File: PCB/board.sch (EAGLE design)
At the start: 43 parts, among them J1 USB-A_PTH_MALE, U1 CH340E, U2 NRF52832, Y1 32MHz_2016, Y2 32.768kHz

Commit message: output files, dir cleanup
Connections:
- net UART_RX: now also U1.RX; no longer U1.TX
- net UART_TX: now also U1.TX; no longer U1.RX
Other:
- moved on the sheet: D1
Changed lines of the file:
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@@
 </classes>
 <parts>
-<part name="SUPPLY2" library="angrypig7-Symbols" deviceset="3V3" device=""/>
-<part name="GND1" library="angrypig7-Symbols" deviceset="GND" device=""/>
-<part name="SUPPLY3" library="angrypig7-Symbols" deviceset="5V" device=""/>
-<part name="SUPPLY4" library="angrypig7-Symbols" deviceset="VIN" device=""/>
-<part name="GND2" library="angrypig7-Symbols" deviceset="GND" device=""/>
-<part name="GND3" library="angrypig7-Symbols" deviceset="GND" device=""/>
 <part name="U2" library="angrypig7-IC-MCU" deviceset="NRF52832" device="" package3d_urn="urn:adsk.eagle:package:25776865/5">
 <attribute name="JLC_ROTATION" value="270"/>
@@
 </plain>
 <instances>
-<instance part="SUPPLY2" gate="G$1" x="27.94" y="21.59" smashed="yes">
-<attribute name="VALUE" x="27.94" y="24.384" size="1.778" layer="96" align="bottom-center"/>
-</instance>
-<instance part="GND1" gate="1" x="27.94" y="15.24" smashed="yes">
-<attribute name="VALUE" x="27.94" y="12.446" size="1.778" layer="96" align="top-center"/>
-</instance>
-<instance part="SUPPLY3" gate="G$1" x="21.59" y="21.59" smashed="yes">
-<attribute name="VALUE" x="21.59" y="24.384" size="1.778" layer="96" align="bottom-center"/>
-</instance>
-<instance part="SUPPLY4" gate="G$1" x="15.24" y="21.59" smashed="yes">
-<attribute name="VALUE" x="15.24" y="24.384" size="1.778" layer="96" align="bottom-center"/>
-</instance>
-<instance part="GND2" gate="1" x="21.59" y="15.24" smashed="yes">
-<attribute name="VALUE" x="21.59" y="12.446" size="1.778" layer="96" align="top-center"/>
-</instance>
-<instance part="GND3" gate="1" x="15.24" y="15.24" smashed="yes">
-<attribute name="VALUE" x="15.24" y="12.446" size="1.778" layer="96" align="top-center"/>
-</instance>
 <instance part="J1" gate="G$1" x="102.87" y="199.39" smashed="yes">
 <attribute name="NAME" x="97.79" y="209.804" size="1.778" layer="95" font="vector"/>
@@
 <attribute name="LCSC" x="102.87" y="199.39" size="1.778" layer="96" display="off"/>
 </instance>
-<instance part="SUPPLY1" gate="G$1" x="157.48" y="212.09" smashed="yes">
-<attribute name="VALUE" x="157.48" y="214.884" size="1.778" layer="96" align="bottom-center"/>
+<instance part="SUPPLY1" gate="G$1" x="157.48" y="214.63" smashed="yes">
+<attribute name="VALUE" x="157.48" y="217.424" size="1.778" layer="96" align="bottom-center"/>
 </instance>
 <instance part="GND4" gate="1" x="120.65" y="190.5" smashed="yes">
@@
 <attribute name="VALUE" x="99.06" y="185.166" size="1.778" layer="96" align="top-center"/>
 </instance>
-<instance part="D1" gate="G$1" x="148.59" y="209.55" smashed="yes">
-<attribute name="NAME" x="146.05" y="211.582" size="1.778" layer="95"/>
-<attribute name="VALUE" x="146.05" y="207.518" size="1.778" layer="96" align="top-left"/>
-<attribute name="LCSC" x="148.59" y="209.55" size="1.27" layer="96" display="off"/>
+<instance part="D1" gate="G$1" x="148.59" y="212.09" smashed="yes">
+<attribute name="NAME" x="146.05" y="214.122" size="1.778" layer="95"/>
+<attribute name="VALUE" x="146.05" y="210.058" size="1.778" layer="96" align="top-left"/>
+<attribute name="LCSC" x="148.59" y="212.09" size="1.27" layer="96" display="off"/>
 </instance>
 <instance part="SUPPLY5" gate="G$1" x="194.31" y="210.82" smashed="yes">
@@
 <segment>
 <pinref part="J1" gate="G$1" pin="D-"/>
-<label x="120.65" y="200.66" size="1.27" layer="95" xref="yes"/>
 <pinref part="D2" gate="G$1" pin="IO3"/>
 <wire x1="139.7" y1="204.47" x2="139.7" y2="207.01" width="0.1524" layer="91"/>
@@
 <segment>
 <pinref part="J1" gate="G$1" pin="D+"/>
-<label x="120.65" y="198.12" size="1.27" layer="95" xref="yes"/>
 <wire x1="113.03" y1="198.12" x2="130.81" y2="198.12" width="0.1524" layer="91"/>
 <wire x1="130.81" y1="198.12" x2="130.81" y2="180.34" width="0.1524" layer="91"/>
@@
 <pinref part="J1" gate="G$1" pin="VBUS"/>
 <wire x1="113.03" y1="203.2" x2="120.65" y2="203.2" width="0.1524" layer="91"/>
-<wire x1="120.65" y1="203.2" x2="120.65" y2="209.55" width="0.1524" layer="91"/>
-<wire x1="120.65" y1="209.55" x2="142.24" y2="209.55" width="0.1524" layer="91"/>
+<wire x1="120.65" y1="203.2" x2="120.65" y2="212.09" width="0.1524" layer="91"/>
+<wire x1="120.65" y1="212.09" x2="142.24" y2="212.09" width="0.1524" layer="91"/>
 <pinref part="D1" gate="G$1" pin="A"/>
 <pinref part="D2" gate="G$1" pin="VCC"/>
-<wire x1="142.24" y1="209.55" x2="146.05" y2="209.55" width="0.1524" layer="91"/>
+<wire x1="142.24" y1="212.09" x2="146.05" y2="212.09" width="0.1524" layer="91"/>
 <wire x1="138.43" y1="200.66" x2="142.24" y2="200.66" width="0.1524" layer="91"/>
-<wire x1="142.24" y1="200.66" x2="142.24" y2="209.55" width="0.1524" layer="91"/>
-<junction x="142.24" y="209.55"/>
+<wire x1="142.24" y1="200.66" x2="142.24" y2="212.09" width="0.1524" layer="91"/>
+<junction x="142.24" y="212.09"/>
 <wire x1="137.16" y1="204.47" x2="137.16" y2="205.74" width="0.1524" layer="91"/>
 <wire x1="137.16" y1="205.74" x2="138.43" y2="205.74" width="0.1524" layer="91"/>
@@
 <pinref part="D1" gate="G$1" pin="C"/>
 <pinref part="SUPPLY1" gate="G$1" pin="5V"/>
-<wire x1="151.13" y1="209.55" x2="157.48" y2="209.55" width="0.1524" layer="91"/>
-<wire x1="157.48" y1="209.55" x2="157.48" y2="212.09" width="0.1524" layer="91"/>
+<wire x1="151.13" y1="212.09" x2="157.48" y2="212.09" width="0.1524" layer="91"/>
+<wire x1="157.48" y1="212.09" x2="157.48" y2="214.63" width="0.1524" layer="91"/>
 </segment>
 <segment>
@@
 <net name="UART_RX" class="0">
 <segment>
+<wire x1="275.59" y1="123.19" x2="266.7" y2="123.19" width="0.1524" layer="91"/>
+<label x="266.7" y="123.19" size="1.27" layer="95" rot="R180" xref="yes"/>
+<pinref part="JP1" gate="A" pin="4"/>
+</segment>
+<segment>
+<label x="187.96" y="127" size="1.27" layer="95" xref="yes"/>
+<pinref part="U1" gate="G$1" pin="RX"/>
+<wire x1="187.96" y1="127" x2="180.34" y2="127" width="0.1524" layer="91"/>
+</segment>
+</net>
+<net name="UART_TX" class="0">
+<segment>
+<wire x1="275.59" y1="125.73" x2="266.7" y2="125.73" width="0.1524" layer="91"/>
+<label x="266.7" y="125.73" size="1.27" layer="95" rot="R180" xref="yes"/>
+<pinref part="JP1" gate="A" pin="3"/>
+</segment>
+<segment>
 <label x="187.96" y="124.46" size="1.27" layer="95" xref="yes"/>
 <pinref part="U1" gate="G$1" pin="TX"/>
 <wire x1="187.96" y1="124.46" x2="180.34" y2="124.46" width="0.1524" layer="91"/>
 </segment>
-<segment>
-<wire x1="275.59" y1="123.19" x2="266.7" y2="123.19" width="0.1524" layer="91"/>
-<label x="266.7" y="123.19" size="1.27" layer="95" rot="R180" xref="yes"/>
-<pinref part="JP1" gate="A" pin="4"/>
-</segment>
-</net>
-<net name="UART_TX" class="0">
-<segment>
-<label x="187.96" y="127" size="1.27" layer="95" xref="yes"/>
-<pinref part="U1" gate="G$1" pin="RX"/>
-<wire x1="187.96" y1="127" x2="180.34" y2="127" width="0.1524" layer="91"/>
-</segment>
-<segment>
-<wire x1="275.59" y1="125.73" x2="266.7" y2="125.73" width="0.1524" layer="91"/>
-<label x="266.7" y="125.73" size="1.27" layer="95" rot="R180" xref="yes"/>
-<pinref part="JP1" gate="A" pin="3"/>
-</segment>
-</net>
+</net>

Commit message: airwire error fix
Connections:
- net UART_RX: now also U1.TX; no longer U1.RX
- net UART_TX: now also U1.RX; no longer U1.TX
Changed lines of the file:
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@@
 </segment>
 <segment>
-<label x="187.96" y="127" size="1.27" layer="95" xref="yes"/>
-<pinref part="U1" gate="G$1" pin="RX"/>
-<wire x1="187.96" y1="127" x2="180.34" y2="127" width="0.1524" layer="91"/>
+<label x="187.96" y="124.46" size="1.27" layer="95" xref="yes"/>
+<wire x1="187.96" y1="124.46" x2="180.34" y2="124.46" width="0.1524" layer="91"/>
+<pinref part="U1" gate="G$1" pin="TX"/>
 </segment>
 </net>
@@
 </segment>
 <segment>
-<label x="187.96" y="124.46" size="1.27" layer="95" xref="yes"/>
-<pinref part="U1" gate="G$1" pin="TX"/>
-<wire x1="187.96" y1="124.46" x2="180.34" y2="124.46" width="0.1524" layer="91"/>
+<label x="187.96" y="127" size="1.27" layer="95" xref="yes"/>
+<wire x1="187.96" y1="127" x2="180.34" y2="127" width="0.1524" layer="91"/>
+<pinref part="U1" gate="G$1" pin="RX"/>
 </segment>
 </net>

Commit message: fixed #7, replaced USB connector part.# on BOM
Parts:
- J1: LCSC C98125 -> C9739
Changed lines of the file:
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@@
 </part>
 <part name="J1" library="angrypig7-Connectors-USB" deviceset="USB-A" device="_PTH_MALE-U-G-O4DD-W-1" override_package3d_urn="urn:adsk.eagle:package:25895599/4" override_package_urn="urn:adsk.eagle:footprint:25895600/1" override_locally_modified="yes" value="USB-A_PTH_MALE">
-<attribute name="LCSC" value="C98125"/>
+<attribute name="LCSC" value="C9739"/>
 </part>
 <part name="SUPPLY1" library="angrypig7-Symbols" deviceset="5V" device=""/>

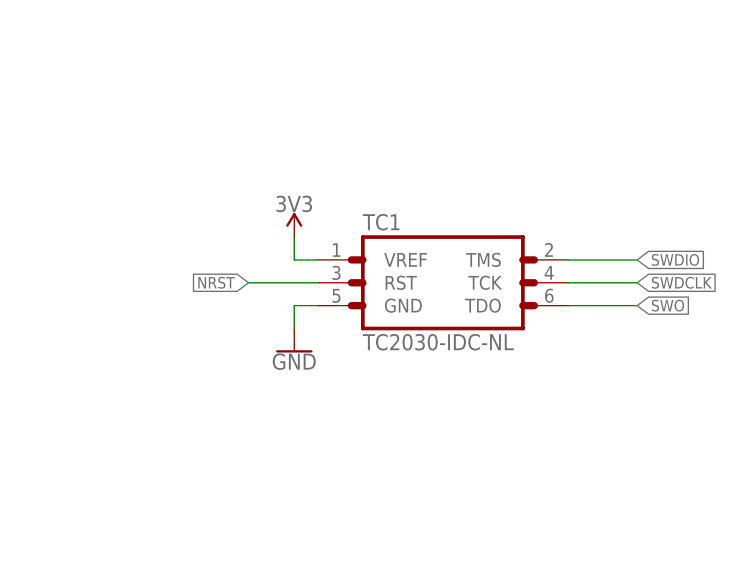
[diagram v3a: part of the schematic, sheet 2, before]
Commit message: PCB trace width DFM
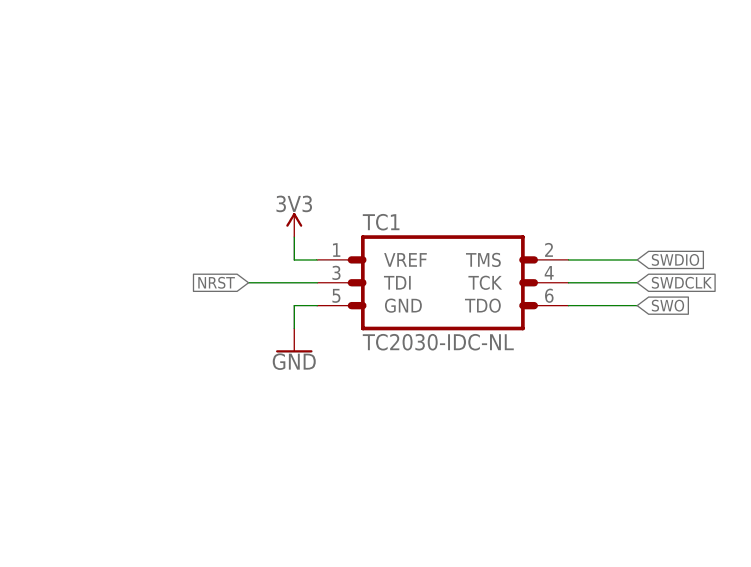
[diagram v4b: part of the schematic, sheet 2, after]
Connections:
- net NRST: now also TC1.TDI; no longer TC1.RST
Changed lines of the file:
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@@
 <wire x1="337.82" y1="86.36" x2="330.2" y2="86.36" width="0.1524" layer="91"/>
 <label x="330.2" y="86.36" size="1.27" layer="95" rot="R180" xref="yes"/>
-<pinref part="TC1" gate="A" pin="RST"/>
+<pinref part="TC1" gate="A" pin="TDI"/>
 </segment>
 </net>
